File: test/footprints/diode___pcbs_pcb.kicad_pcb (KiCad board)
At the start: 2 copper layers, 1 part

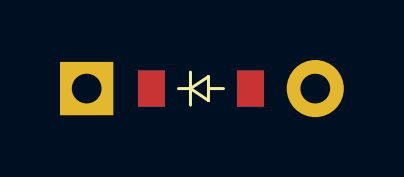
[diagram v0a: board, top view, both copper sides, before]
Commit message: Allow diode SMD/THT footprints to be disabled
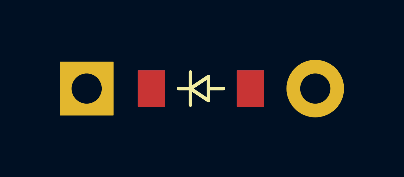
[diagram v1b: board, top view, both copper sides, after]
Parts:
- added D2, D3: , ComboDiode, F.Cu at (0.00, 0.00)
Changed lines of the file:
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@@
 (add_net "to")
   )
-    (module ComboDiode (layer F.Cu)
+      (module ComboDiode (layer F.Cu)
         (at 0 0 0)
         (fp_text reference "D1" (at 0 0) (layer F.SilkS) hide (effects (font (size 1.27 1.27) (thickness 0.15))))
@@
         (fp_line (start -0.35 0) (end -0.35 -0.55) (layer B.SilkS) (width 0.1))
         (fp_line (start -0.75 0) (end -0.35 0) (layer B.SilkS) (width 0.1))
-        (pad 1 smd rect (at -1.65 0 0) (size 0.9 1.2) (layers F.Cu F.Paste F.Mask) (net 2 "to"))
-        (pad 2 smd rect (at 1.65 0 0) (size 0.9 1.2) (layers B.Cu B.Paste B.Mask) (net 1 "from"))
-        (pad 1 smd rect (at -1.65 0 0) (size 0.9 1.2) (layers B.Cu B.Paste B.Mask) (net 2 "to"))
-        (pad 2 smd rect (at 1.65 0 0) (size 0.9 1.2) (layers F.Cu F.Paste F.Mask) (net 1 "from"))
-        (pad 1 thru_hole rect (at -3.81 0 0) (size 1.778 1.778) (drill 0.9906) (layers *.Cu *.Mask) (net 2 "to"))
-        (pad 2 thru_hole circle (at 3.81 0 0) (size 1.905 1.905) (drill 0.9906) (layers *.Cu *.Mask) (net 1 "from"))
-    )
+      (pad 1 smd rect (at -1.65 0 0) (size 0.9 1.2) (layers F.Cu F.Paste F.Mask) (net 2 "to"))
+      (pad 2 smd rect (at 1.65 0 0) (size 0.9 1.2) (layers B.Cu B.Paste B.Mask) (net 1 "from"))
+      (pad 1 smd rect (at -1.65 0 0) (size 0.9 1.2) (layers B.Cu B.Paste B.Mask) (net 2 "to"))
+      (pad 2 smd rect (at 1.65 0 0) (size 0.9 1.2) (layers F.Cu F.Paste F.Mask) (net 1 "from"))
+      (pad 1 thru_hole rect (at -3.81 0 0) (size 1.778 1.778) (drill 0.9906) (layers *.Cu *.Mask) (net 2 "to"))
+      (pad 2 thru_hole circle (at 3.81 0 0) (size 1.905 1.905) (drill 0.9906) (layers *.Cu *.Mask) (net 1 "from"))
+      )
+      (module ComboDiode (layer F.Cu)
+        (at 0 0 0)
+        (fp_text reference "D2" (at 0 0) (layer F.SilkS) hide (effects (font (size 1.27 1.27) (thickness 0.15))))
+        (fp_text value "" (at 0 0) (layer F.SilkS) hide (effects (font (size 1.27 1.27) (thickness 0.15))))
+        (fp_line (start 0.25 0) (end 0.75 0) (layer F.SilkS) (width 0.1))
+        (fp_line (start 0.25 0.4) (end -0.35 0) (layer F.SilkS) (width 0.1))
+        (fp_line (start 0.25 -0.4) (end 0.25 0.4) (layer F.SilkS) (width 0.1))
+        (fp_line (start -0.35 0) (end 0.25 -0.4) (layer F.SilkS) (width 0.1))
+        (fp_line (start -0.35 0) (end -0.35 0.55) (layer F.SilkS) (width 0.1))
+        (fp_line (start -0.35 0) (end -0.35 -0.55) (layer F.SilkS) (width 0.1))
+        (fp_line (start -0.75 0) (end -0.35 0) (layer F.SilkS) (width 0.1))
+        (fp_line (start 0.25 0) (end 0.75 0) (layer B.SilkS) (width 0.1))
+        (fp_line (start 0.25 0.4) (end -0.35 0) (layer B.SilkS) (width 0.1))
+        (fp_line (start 0.25 -0.4) (end 0.25 0.4) (layer B.SilkS) (width 0.1))
+        (fp_line (start -0.35 0) (end 0.25 -0.4) (layer B.SilkS) (width 0.1))
+        (fp_line (start -0.35 0) (end -0.35 0.55) (layer B.SilkS) (width 0.1))
+        (fp_line (start -0.35 0) (end -0.35 -0.55) (layer B.SilkS) (width 0.1))
+        (fp_line (start -0.75 0) (end -0.35 0) (layer B.SilkS) (width 0.1))
+      (pad 1 thru_hole rect (at -3.81 0 0) (size 1.778 1.778) (drill 0.9906) (layers *.Cu *.Mask) (net 2 "to"))
+      (pad 2 thru_hole circle (at 3.81 0 0) (size 1.905 1.905) (drill 0.9906) (layers *.Cu *.Mask) (net 1 "from"))
+      )
+      (module ComboDiode (layer F.Cu)
+        (at 0 0 0)
+        (fp_text reference "D3" (at 0 0) (layer F.SilkS) hide (effects (font (size 1.27 1.27) (thickness 0.15))))
+        (fp_text value "" (at 0 0) (layer F.SilkS) hide (effects (font (size 1.27 1.27) (thickness 0.15))))
+        (fp_line (start 0.25 0) (end 0.75 0) (layer F.SilkS) (width 0.1))
+        (fp_line (start 0.25 0.4) (end -0.35 0) (layer F.SilkS) (width 0.1))
+        (fp_line (start 0.25 -0.4) (end 0.25 0.4) (layer F.SilkS) (width 0.1))
+        (fp_line (start -0.35 0) (end 0.25 -0.4) (layer F.SilkS) (width 0.1))
+        (fp_line (start -0.35 0) (end -0.35 0.55) (layer F.SilkS) (width 0.1))
+        (fp_line (start -0.35 0) (end -0.35 -0.55) (layer F.SilkS) (width 0.1))
+        (fp_line (start -0.75 0) (end -0.35 0) (layer F.SilkS) (width 0.1))
+        (fp_line (start 0.25 0) (end 0.75 0) (layer B.SilkS) (width 0.1))
+        (fp_line (start 0.25 0.4) (end -0.35 0) (layer B.SilkS) (width 0.1))
+        (fp_line (start 0.25 -0.4) (end 0.25 0.4) (layer B.SilkS) (width 0.1))
+        (fp_line (start -0.35 0) (end 0.25 -0.4) (layer B.SilkS) (width 0.1))
+        (fp_line (start -0.35 0) (end -0.35 0.55) (layer B.SilkS) (width 0.1))
+        (fp_line (start -0.35 0) (end -0.35 -0.55) (layer B.SilkS) (width 0.1))
+        (fp_line (start -0.75 0) (end -0.35 0) (layer B.SilkS) (width 0.1))
+      (pad 1 smd rect (at -1.65 0 0) (size 0.9 1.2) (layers F.Cu F.Paste F.Mask) (net 2 "to"))
+      (pad 2 smd rect (at 1.65 0 0) (size 0.9 1.2) (layers B.Cu B.Paste B.Mask) (net 1 "from"))
+      (pad 1 smd rect (at -1.65 0 0) (size 0.9 1.2) (layers B.Cu B.Paste B.Mask) (net 2 "to"))
+      (pad 2 smd rect (at 1.65 0 0) (size 0.9 1.2) (layers F.Cu F.Paste F.Mask) (net 1 "from"))
+      )
 )

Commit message: Add internal vias option to diodes
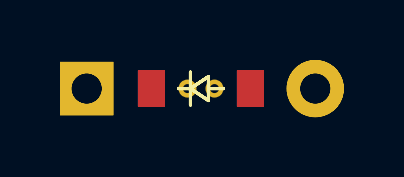
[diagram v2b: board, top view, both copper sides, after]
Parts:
- added D4: , ComboDiode, F.Cu at (0.00, 0.00)
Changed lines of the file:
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@@
       (pad 2 smd rect (at 1.65 0 0) (size 0.9 1.2) (layers F.Cu F.Paste F.Mask) (net 1 "from"))
       )
+      (module ComboDiode (layer F.Cu)
+        (at 0 0 0)
+        (fp_text reference "D4" (at 0 0) (layer F.SilkS) hide (effects (font (size 1.27 1.27) (thickness 0.15))))
+        (fp_text value "" (at 0 0) (layer F.SilkS) hide (effects (font (size 1.27 1.27) (thickness 0.15))))
+        (fp_line (start 0.25 0) (end 0.75 0) (layer F.SilkS) (width 0.1))
+        (fp_line (start 0.25 0.4) (end -0.35 0) (layer F.SilkS) (width 0.1))
+        (fp_line (start 0.25 -0.4) (end 0.25 0.4) (layer F.SilkS) (width 0.1))
+        (fp_line (start -0.35 0) (end 0.25 -0.4) (layer F.SilkS) (width 0.1))
+        (fp_line (start -0.35 0) (end -0.35 0.55) (layer F.SilkS) (width 0.1))
+        (fp_line (start -0.35 0) (end -0.35 -0.55) (layer F.SilkS) (width 0.1))
+        (fp_line (start -0.75 0) (end -0.35 0) (layer F.SilkS) (width 0.1))
+        (fp_line (start 0.25 0) (end 0.75 0) (layer B.SilkS) (width 0.1))
+        (fp_line (start 0.25 0.4) (end -0.35 0) (layer B.SilkS) (width 0.1))
+        (fp_line (start 0.25 -0.4) (end 0.25 0.4) (layer B.SilkS) (width 0.1))
+        (fp_line (start -0.35 0) (end 0.25 -0.4) (layer B.SilkS) (width 0.1))
+        (fp_line (start -0.35 0) (end -0.35 0.55) (layer B.SilkS) (width 0.1))
+        (fp_line (start -0.35 0) (end -0.35 -0.55) (layer B.SilkS) (width 0.1))
+        (fp_line (start -0.75 0) (end -0.35 0) (layer B.SilkS) (width 0.1))
+      (pad 1 smd rect (at -1.65 0 0) (size 0.9 1.2) (layers F.Cu F.Paste F.Mask) (net 2 "to"))
+      (pad 2 smd rect (at 1.65 0 0) (size 0.9 1.2) (layers B.Cu B.Paste B.Mask) (net 1 "from"))
+      (pad 1 smd rect (at -1.65 0 0) (size 0.9 1.2) (layers B.Cu B.Paste B.Mask) (net 2 "to"))
+      (pad 2 smd rect (at 1.65 0 0) (size 0.9 1.2) (layers F.Cu F.Paste F.Mask) (net 1 "from"))
+      (pad 1 thru_hole circle (at -0.45 0) (size 0.6 0.6) (drill 0.3) (layers *.Cu) (net 2 "to"))
+      (pad 2 thru_hole circle (at 0.45 0) (size 0.6 0.6) (drill 0.3) (layers *.Cu) (net 1 "from"))
+      )
 )

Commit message: Add via in pad option for diodes
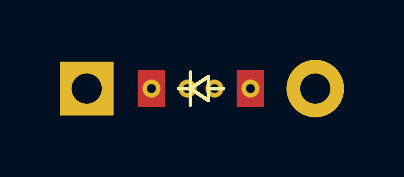
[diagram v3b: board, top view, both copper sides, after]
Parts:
- added D5: , ComboDiode, F.Cu at (0.00, 0.00)
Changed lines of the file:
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@@
       (pad 1 smd rect (at -1.65 0 0) (size 0.9 1.2) (layers B.Cu B.Paste B.Mask) (net 2 "to"))
       (pad 2 smd rect (at 1.65 0 0) (size 0.9 1.2) (layers F.Cu F.Paste F.Mask) (net 1 "from"))
-      (pad 1 thru_hole circle (at -0.45 0) (size 0.6 0.6) (drill 0.3) (layers *.Cu) (net 2 "to"))
-      (pad 2 thru_hole circle (at 0.45 0) (size 0.6 0.6) (drill 0.3) (layers *.Cu) (net 1 "from"))
+        (pad 1 thru_hole circle (at -0.45 0) (size 0.6 0.6) (drill 0.3) (layers *.Cu) (net 2 "to"))
+        (pad 2 thru_hole circle (at 0.45 0) (size 0.6 0.6) (drill 0.3) (layers *.Cu) (net 1 "from"))
+      )
+      (module ComboDiode (layer F.Cu)
+        (at 0 0 0)
+        (fp_text reference "D5" (at 0 0) (layer F.SilkS) hide (effects (font (size 1.27 1.27) (thickness 0.15))))
+        (fp_text value "" (at 0 0) (layer F.SilkS) hide (effects (font (size 1.27 1.27) (thickness 0.15))))
+        (fp_line (start 0.25 0) (end 0.75 0) (layer F.SilkS) (width 0.1))
+        (fp_line (start 0.25 0.4) (end -0.35 0) (layer F.SilkS) (width 0.1))
+        (fp_line (start 0.25 -0.4) (end 0.25 0.4) (layer F.SilkS) (width 0.1))
+        (fp_line (start -0.35 0) (end 0.25 -0.4) (layer F.SilkS) (width 0.1))
+        (fp_line (start -0.35 0) (end -0.35 0.55) (layer F.SilkS) (width 0.1))
+        (fp_line (start -0.35 0) (end -0.35 -0.55) (layer F.SilkS) (width 0.1))
+        (fp_line (start -0.75 0) (end -0.35 0) (layer F.SilkS) (width 0.1))
+        (fp_line (start 0.25 0) (end 0.75 0) (layer B.SilkS) (width 0.1))
+        (fp_line (start 0.25 0.4) (end -0.35 0) (layer B.SilkS) (width 0.1))
+        (fp_line (start 0.25 -0.4) (end 0.25 0.4) (layer B.SilkS) (width 0.1))
+        (fp_line (start -0.35 0) (end 0.25 -0.4) (layer B.SilkS) (width 0.1))
+        (fp_line (start -0.35 0) (end -0.35 0.55) (layer B.SilkS) (width 0.1))
+        (fp_line (start -0.35 0) (end -0.35 -0.55) (layer B.SilkS) (width 0.1))
+        (fp_line (start -0.75 0) (end -0.35 0) (layer B.SilkS) (width 0.1))
+      (pad 1 smd rect (at -1.65 0 0) (size 0.9 1.2) (layers F.Cu F.Paste F.Mask) (net 2 "to"))
+      (pad 2 smd rect (at 1.65 0 0) (size 0.9 1.2) (layers B.Cu B.Paste B.Mask) (net 1 "from"))
+      (pad 1 smd rect (at -1.65 0 0) (size 0.9 1.2) (layers B.Cu B.Paste B.Mask) (net 2 "to"))
+      (pad 2 smd rect (at 1.65 0 0) (size 0.9 1.2) (layers F.Cu F.Paste F.Mask) (net 1 "from"))
+        (pad 1 thru_hole circle (at -1.65 0) (size 0.6 0.6) (drill 0.3) (layers *.Cu) (net 2 "to"))
+        (pad 2 thru_hole circle (at 1.65 0) (size 0.6 0.6) (drill 0.3) (layers *.Cu) (net 1 "from"))
       )
 )
